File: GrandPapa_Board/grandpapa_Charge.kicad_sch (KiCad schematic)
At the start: 22 parts, among them J1 3.7V LiPo Single Cell, U3 MCP73871T-1CCI/ML, U4 INA180

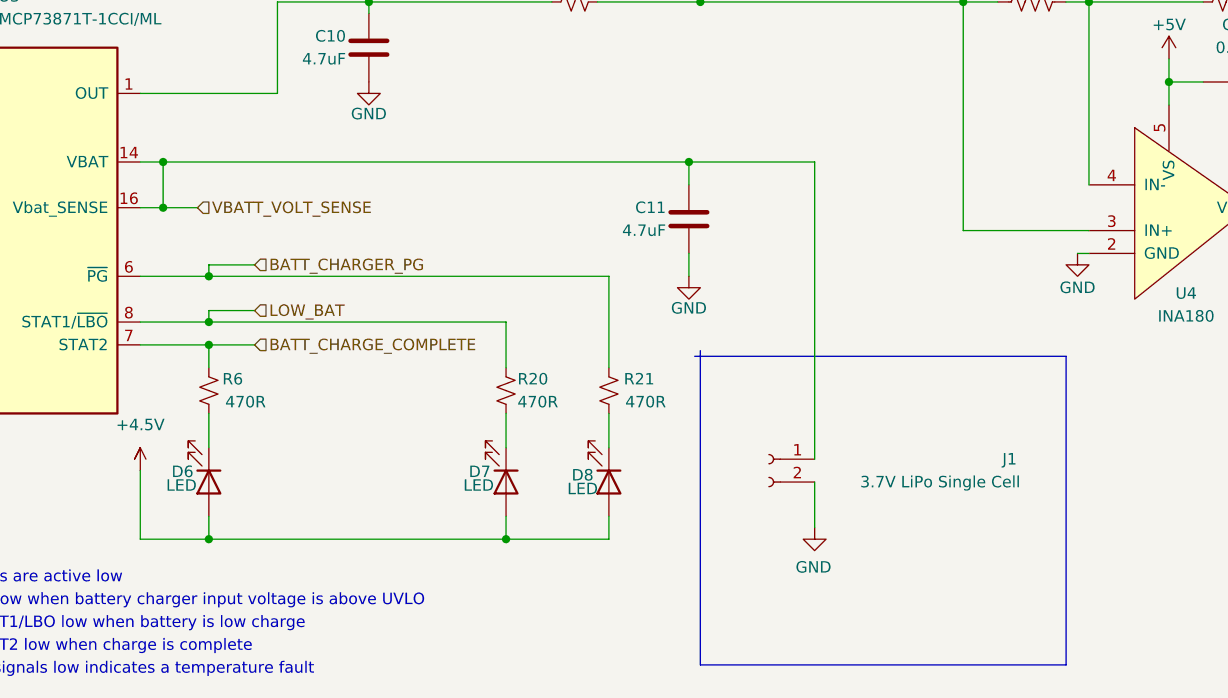
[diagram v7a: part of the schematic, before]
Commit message: minor changes, change some buck converter component values, add inductor + LED part numbers
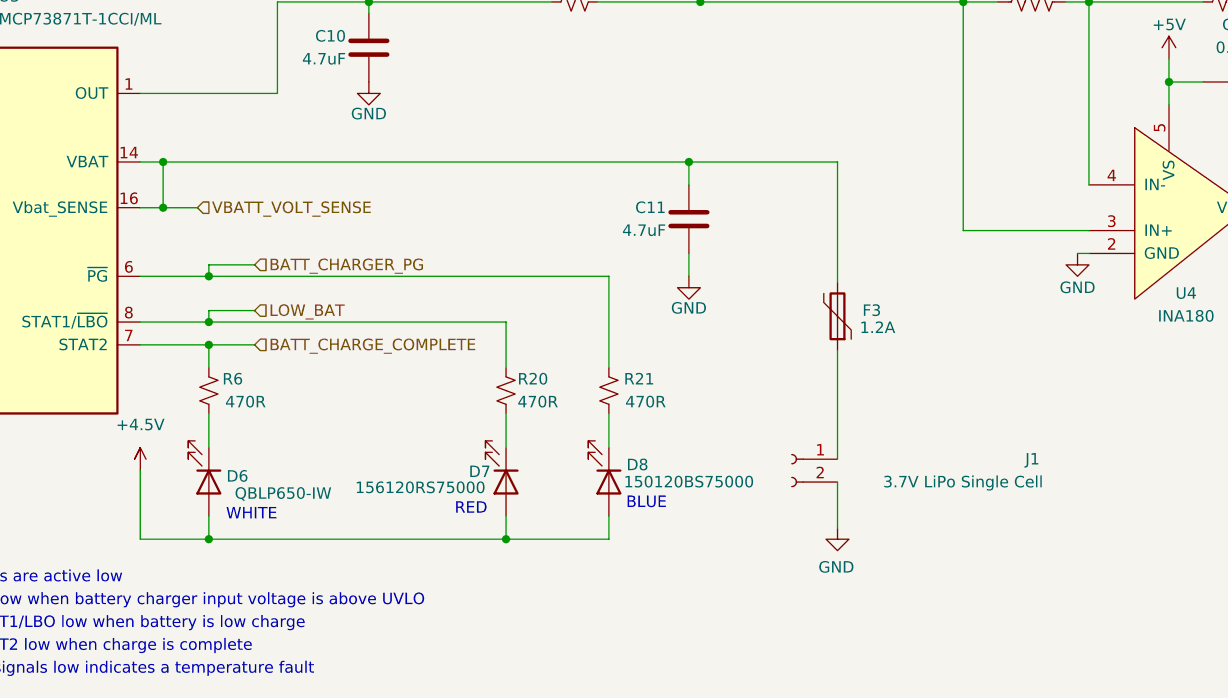
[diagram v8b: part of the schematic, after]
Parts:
- added F3: 1.2A, symbol Device:Polyfuse
- D6: value LED -> QBLP650-IW
- D7: value LED -> 156120RS75000
- D8: value LED -> 150120BS75000
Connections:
- net VBATT_VOLT_SENSE: now also F3.2; no longer J1.1 (Pin_1)
- new net: F3.1, J1.1 (Pin_1)
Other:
- note added: "BLUE"
- note added: "RED"
- note added: "WHITE"
- moved on the sheet: J1
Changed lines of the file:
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@@
+    (stroke (width 0) (type default) (color 0 0 0 0))
+  )
+  (wire (pts (xy 187.96 108.585) (xy 187.96 120.65))
     (stroke (width 0) (type default) (color 0 0 0 0))
   )
@@
     (stroke (width 0) (type default) (color 0 0 0 0))
   )
-  (polyline (pts (xy 172.72 108.585) (xy 172.72 143.51))
-    (stroke (width 0) (type default) (color 0 0 0 0))
-  )
   (wire (pts (xy 56.515 100.33) (xy 59.69 100.33))
     (stroke (width 0) (type default) (color 0 0 0 0))
@@
     (stroke (width 0) (type default) (color 0 0 0 0))
   )
-  (polyline (pts (xy 213.36 143.51) (xy 172.72 143.51))
-    (stroke (width 0) (type default) (color 0 0 0 0))
-  )
   (wire (pts (xy 224.79 78.74) (xy 228.6 78.74))
     (stroke (width 0) (type default) (color 0 0 0 0))
@@
     (stroke (width 0) (type default) (color 0 0 0 0))
   )
-  (wire (pts (xy 185.42 87.63) (xy 185.42 120.65))
+  (wire (pts (xy 187.96 87.63) (xy 187.96 100.965))
     (stroke (width 0) (type default) (color 0 0 0 0))
   )
@@
     (stroke (width 0) (type default) (color 0 0 0 0))
   )
-  (polyline (pts (xy 213.36 109.22) (xy 213.36 143.51))
-    (stroke (width 0) (type default) (color 0 0 0 0))
-  )
   (wire (pts (xy 171.45 97.79) (xy 171.45 100.33))
     (stroke (width 0) (type default) (color 0 0 0 0))
@@
     (stroke (width 0) (type default) (color 0 0 0 0))
   )
-  (polyline (pts (xy 172.085 109.22) (xy 213.36 109.22))
-    (stroke (width 0) (type default) (color 0 0 0 0))
-  )
   (wire (pts (xy 213.36 69.85) (xy 215.9 69.85))
     (stroke (width 0) (type default) (color 0 0 0 0))
@@
     (stroke (width 0) (type default) (color 0 0 0 0))
   )
-  (wire (pts (xy 171.45 87.63) (xy 185.42 87.63))
+  (wire (pts (xy 171.45 87.63) (xy 187.96 87.63))
     (stroke (width 0) (type default) (color 0 0 0 0))
   )
@@
     (stroke (width 0) (type default) (color 0 0 0 0))
   )
-  (wire (pts (xy 185.42 123.19) (xy 185.42 128.27))
+  (wire (pts (xy 187.96 123.19) (xy 187.96 128.27))
     (stroke (width 0) (type default) (color 0 0 0 0))
   )
@@
     (stroke (width 0) (type default) (color 0 0 0 0))
   )
+  (text "BLUE" (at 164.465 126.365 0)
+    (effects (font (size 1.27 1.27)) (justify left bottom))
+  )
   (text "All signals low indicates a temperature fault\n" (at 91.44 144.78 0)
     (effects (font (size 1.27 1.27)) (justify left bottom))
@@
   )
   (text "3.7V to 4.5V" (at 259.08 62.23 0)
+    (effects (font (size 1.27 1.27)) (justify left bottom))
+  )
+  (text "RED" (at 145.415 127 0)
     (effects (font (size 1.27 1.27)) (justify left bottom))
   )
@@
   (text "BATTERY CHARGE IC\n" (at 78.994 49.149 0)
     (effects (font (size 2 2) (thickness 0.4) bold) (justify left bottom))
+  )
+  (text "WHITE\n" (at 120.015 127.635 0)
+    (effects (font (size 1.27 1.27)) (justify left bottom))
   )
   (text "LIPO charge voltage = 4.1V, 4.121V MAX\nFast charge current = 1000V/Rprog1 = 1000/2kOhm = 500mA\nTimer disabled\nCharger always enabled\nTHERM curr = 50uA, shutdown happens at 1.24V and 0.25V\n"
@@
     (pin "1")
   )
-  (symbol (lib_id "power:GND") (at 185.42 128.27 0) (mirror y) (unit 1)
-    (in_bom yes) (on_board yes)
-    (property "Reference" "#PWR024" (id 0) (at 185.42 134.62 0)
-      (effects (font (size 1.27 1.27)) hide)
-    )
-    (property "Value" "GND" (id 1) (at 185.293 132.6642 0))
-    (property "Footprint" "" (id 2) (at 185.42 128.27 0)
-      (effects (font (size 1.27 1.27)) hide)
-    )
-    (property "Datasheet" "" (id 3) (at 185.42 128.27 0)
+  (symbol (lib_id "power:GND") (at 187.96 128.27 0) (mirror y) (unit 1)
+    (in_bom yes) (on_board yes)
+    (property "Reference" "#PWR024" (id 0) (at 187.96 134.62 0)
+      (effects (font (size 1.27 1.27)) hide)
+    )
+    (property "Value" "GND" (id 1) (at 187.833 132.6642 0))
+    (property "Footprint" "" (id 2) (at 187.96 128.27 0)
+      (effects (font (size 1.27 1.27)) hide)
+    )
+    (property "Datasheet" "" (id 3) (at 187.96 128.27 0)
       (effects (font (size 1.27 1.27)) hide)
     )
@@
     (pin "2")
   )
-  (symbol (lib_id "Connector:Conn_01x02_Female") (at 180.34 120.65 0) (mirror y) (unit 1)
-    (in_bom yes) (on_board yes)
-    (property "Reference" "J1" (id 0) (at 207.899 120.65 0)
-      (effects (font (size 1.27 1.27)) (justify left))
-    )
-    (property "Value" "3.7V LiPo Single Cell" (id 1) (at 208.28 123.19 0)
-      (effects (font (size 1.27 1.27)) (justify left))
-    )
-    (property "Footprint" "Connector_JST:JST_PH_S2B-PH-K_1x02_P2.00mm_Horizontal" (id 2) (at 180.34 120.65 0)
-      (effects (font (size 1.27 1.27)) hide)
-    )
-    (property "Datasheet" "~" (id 3) (at 180.34 120.65 0)
+  (symbol (lib_id "Connector:Conn_01x02_Female") (at 182.88 120.65 0) (mirror y) (unit 1)
+    (in_bom yes) (on_board yes)
+    (property "Reference" "J1" (id 0) (at 210.439 120.65 0)
+      (effects (font (size 1.27 1.27)) (justify left))
+    )
+    (property "Value" "3.7V LiPo Single Cell" (id 1) (at 210.82 123.19 0)
+      (effects (font (size 1.27 1.27)) (justify left))
+    )
+    (property "Footprint" "Connector_JST:JST_PH_S2B-PH-K_1x02_P2.00mm_Horizontal" (id 2) (at 182.88 120.65 0)
+      (effects (font (size 1.27 1.27)) hide)
+    )
+    (property "Datasheet" "~" (id 3) (at 182.88 120.65 0)
       (effects (font (size 1.27 1.27)) hide)
     )
@@
     (pin "5")
   )
+  (symbol (lib_id "Device:Polyfuse") (at 187.96 104.775 180) (unit 1)
+    (in_bom yes) (on_board yes)
+    (property "Reference" "F3" (id 0) (at 191.77 104.14 0))
+    (property "Value" "1.2A" (id 1) (at 192.405 106.045 0))
+    (property "Footprint" "" (id 2) (at 186.69 99.695 0)
+      (effects (font (size 1.27 1.27)) (justify left) hide)
+    )
+    (property "Datasheet" "~" (id 3) (at 187.96 104.775 0)
+      (effects (font (size 1.27 1.27)) hide)
+    )
+    (pin "1")
+    (pin "2")
+  )
   (symbol (lib_id "Device:LED") (at 118.11 123.19 270) (unit 1)
     (in_bom yes) (on_board yes)
-    (property "Reference" "D6" (id 0) (at 115.189 122.047 90))
-    (property "Value" "LED" (id 1) (at 115.062 123.571 90))
+    (property "Reference" "D6" (id 0) (at 121.285 122.555 90))
+    (property "Value" "QBLP650-IW" (id 1) (at 126.365 124.46 90))
     (property "Footprint" "" (id 2) (at 118.11 123.19 0)
       (effects (font (size 1.27 1.27)) hide)
@@
   (symbol (lib_id "Device:LED") (at 162.56 123.19 270) (unit 1)
     (in_bom yes) (on_board yes)
-    (property "Reference" "D8" (id 0) (at 159.639 122.428 90))
-    (property "Value" "LED" (id 1) (at 159.639 123.952 90))
+    (property "Reference" "D8" (id 0) (at 165.735 121.285 90))
+    (property "Value" "150120BS75000" (id 1) (at 171.45 123.19 90))
     (property "Footprint" "" (id 2) (at 162.56 123.19 0)
       (effects (font (size 1.27 1.27)) hide)
@@
     (in_bom yes) (on_board yes)
     (property "Reference" "D7" (id 0) (at 148.209 122.047 90))
-    (property "Value" "LED" (id 1) (at 148.082 123.571 90))
+    (property "Value" "156120RS75000" (id 1) (at 141.605 123.825 90))
     (property "Footprint" "" (id 2) (at 151.13 123.19 0)
       (effects (font (size 1.27 1.27)) hide)
